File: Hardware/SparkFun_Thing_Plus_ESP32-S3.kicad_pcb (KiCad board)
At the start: 4 copper layers, 22.9 x 58.4 mm, 132 parts, among them J1 USB_C_Receptacle, J2 microSD_Friction, J3 JST_2mm_LiPo, J4 Qwiic_Vertical, SW1 4.6x2.8mm, SW2 4.6x2.8mm, U1 AP2112K-3.3, U10 ThingPlus, U2 TVS_ESD_USB, U3 ESP32-S3-MINI, U4 MAX17048, U5 MCP73831, U6 AP2112K-3.3

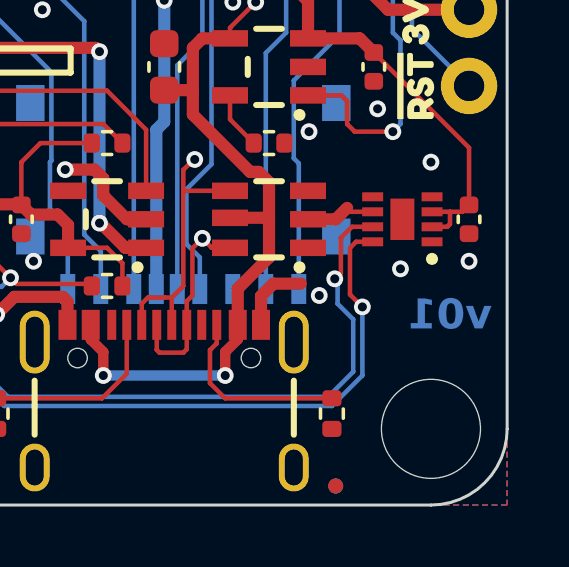
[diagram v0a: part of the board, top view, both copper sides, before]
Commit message: Remove single unit production files
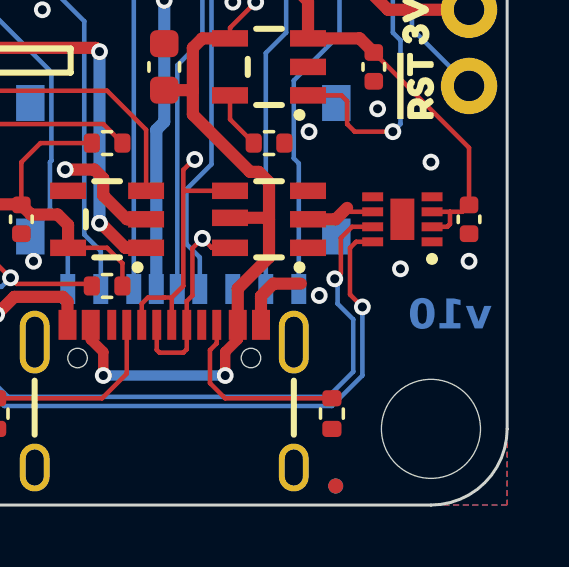
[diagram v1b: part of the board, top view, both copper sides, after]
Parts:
- removed kibuzzard-6569F804: G***, kibuzzard-6569F804
- added kibuzzard-65A403E0: G***, kibuzzard-65A403E0, B.Cu at (113.0, 98.4)
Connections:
- net +3.3V renamed 3.3V
- net +5V renamed 5V
- J3 pad NC1: (no net) -> unconnected-(J3-PadNC1)
- J3 pad NC2: (no net) -> unconnected-(J3-PadNC2)
- U4 pad 9: (no net) -> GND
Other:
- board text added: "Finish: HASL Lead-Free"
- board text added: "v10"
- board text removed: "Finish: ENIG"
- board text removed: "v01"

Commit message: Updates post review
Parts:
- removed kibuzzard-6569FC00: G***, kibuzzard-6569FC00
- removed kibuzzard-6569FC19: G***, kibuzzard-6569FC19
- removed kibuzzard-6569FC2B: G***, kibuzzard-6569FC2B
- removed kibuzzard-6569FC30: G***, kibuzzard-6569FC30
- removed kibuzzard-6569FC40: G***, kibuzzard-6569FC40
- removed kibuzzard-6569FC46: G***, kibuzzard-6569FC46
- removed kibuzzard-6569FC4B: G***, kibuzzard-6569FC4B
- removed kibuzzard-6569FC6D: G***, kibuzzard-6569FC6D
- removed kibuzzard-6569FC75: G***, kibuzzard-6569FC75
- removed kibuzzard-656A1BAC: G***, kibuzzard-656A1BAC
- removed kibuzzard-656A1BFB: G***, kibuzzard-656A1BFB
- removed kibuzzard-656A1C04: G***, kibuzzard-656A1C04
- removed kibuzzard-656A1C15: G***, kibuzzard-656A1C15
- removed kibuzzard-656A1C24: G***, kibuzzard-656A1C24
- removed kibuzzard-656A1C2E: G***, kibuzzard-656A1C2E
- removed kibuzzard-656A1C4C: G***, kibuzzard-656A1C4C
- removed kibuzzard-656A1C93: G***, kibuzzard-656A1C93
- removed kibuzzard-656A1C9C: G***, kibuzzard-656A1C9C
- removed kibuzzard-656A1CA0: G***, kibuzzard-656A1CA0
- removed kibuzzard-656A1CA7: G***, kibuzzard-656A1CA7
- removed kibuzzard-656A1CAC: G***, kibuzzard-656A1CAC
- removed kibuzzard-656A1CB7: G***, kibuzzard-656A1CB7
- removed kibuzzard-656A1CC2: G***, kibuzzard-656A1CC2
- removed kibuzzard-656A1CC7: G***, kibuzzard-656A1CC7
- removed kibuzzard-656A1CEA: G***, kibuzzard-656A1CEA
- removed kibuzzard-656A31BE: G***, kibuzzard-656A31BE
- removed kibuzzard-656A31C7: G***, kibuzzard-656A31C7
- removed kibuzzard-656A36EF: G***, kibuzzard-656A36EF
- removed kibuzzard-656A3874: G***, kibuzzard-656A3874
- removed kibuzzard-656A387C: G***, kibuzzard-656A387C
- removed kibuzzard-656A38AA: G***, kibuzzard-656A38AA
- removed kibuzzard-656A3901: G***, kibuzzard-656A3901
- added LP1: ~, SparkFun-Jumper:SMT-JUMPER_3_1-NC_TRACE_SILK, B.Cu at (116.3, 128.3)
- added Q1: DMG2305UX, SparkFun-Semiconductor-Standard:SOT23-3, F.Cu at (119.4, 129.2)
- added R17: 100k, SparkFun-Resistor:R_0402_1005Metric, F.Cu at (111.1, 139.1)
- added R18: 100k, SparkFun-Resistor:R_0402_1005Metric, F.Cu at (120.0, 131.8)
- added kibuzzard-65A9923A: G***, kibuzzard-65A9923A, B.Cu at (121.0, 100.3)
- added kibuzzard-65A99252: G***, kibuzzard-65A99252, B.Cu at (119.4, 102.9)
- added kibuzzard-65A99268: G***, kibuzzard-65A99268, B.Cu at (119.6, 105.4)
- added kibuzzard-65A9926C: G***, kibuzzard-65A9926C, B.Cu at (119.4, 108.0)
- added kibuzzard-65A9926F: G***, kibuzzard-65A9926F, B.Cu at (119.5, 110.5)
- added kibuzzard-65A99274: G***, kibuzzard-65A99274, B.Cu at (119.6, 113.0)
- added kibuzzard-65A99278: G***, kibuzzard-65A99278, B.Cu at (121.2, 115.6)
- added kibuzzard-65A9927C: G***, kibuzzard-65A9927C, B.Cu at (121.2, 118.1)
- added kibuzzard-65A9927F: G***, kibuzzard-65A9927F, B.Cu at (121.2, 120.7)
- added kibuzzard-65A99283: G***, kibuzzard-65A99283, B.Cu at (121.2, 123.2)
- added kibuzzard-65A99287: G***, kibuzzard-65A99287, B.Cu at (121.2, 125.7)
- added kibuzzard-65A9928A: G***, kibuzzard-65A9928A, B.Cu at (121.0, 128.3)
- added kibuzzard-65A9928E: G***, kibuzzard-65A9928E, B.Cu at (120.8, 130.8)
- added kibuzzard-65A99292: G***, kibuzzard-65A99292, B.Cu at (121.3, 133.3)
- added kibuzzard-65A99297: G***, kibuzzard-65A99297, B.Cu at (120.9, 135.9)
- added kibuzzard-65A992E3: G***, kibuzzard-65A992E3, B.Cu at (123.2, 141.0)
- added kibuzzard-65A99335: G***, kibuzzard-65A99335, B.Cu at (106.3, 100.3)
- added kibuzzard-65A9933C: G***, kibuzzard-65A9933C, B.Cu at (106.2, 102.9)
- added kibuzzard-65A99346: G***, kibuzzard-65A99346, B.Cu at (104.8, 108.0)
- added kibuzzard-65A9934B: G***, kibuzzard-65A9934B, B.Cu at (104.6, 105.4)
- added kibuzzard-65A99350: G***, kibuzzard-65A99350, B.Cu at (104.8, 110.5)
- added kibuzzard-65A99354: G***, kibuzzard-65A99354, B.Cu at (104.6, 113.0)
- added kibuzzard-65A99359: G***, kibuzzard-65A99359, B.Cu at (104.6, 115.6)
- added kibuzzard-65A9935C: G***, kibuzzard-65A9935C, B.Cu at (104.8, 118.1)
- added kibuzzard-65A99360: G***, kibuzzard-65A99360, B.Cu at (105.0, 120.7)
- added kibuzzard-65A99364: G***, kibuzzard-65A99364, B.Cu at (105.7, 123.2)
- added kibuzzard-65A99367: G***, kibuzzard-65A99367, B.Cu at (105.0, 125.7)
- added kibuzzard-65A9936B: G***, kibuzzard-65A9936B, B.Cu at (106.2, 128.3)
- added kibuzzard-65A9990D: G***, kibuzzard-65A9990D, F.Cu at (104.6, 123.2)
- added kibuzzard-65A99912: G***, kibuzzard-65A99912, F.Cu at (104.6, 128.3)
- added kibuzzard-65A99933: G***, kibuzzard-65A99933, B.Cu at (121.9, 96.5)
- added kibuzzard-65A99A9C: G***, kibuzzard-65A99A9C, F.Cu at (110.9, 131.2)
- added kibuzzard-65A99AA3: G***, kibuzzard-65A99AA3, F.Cu at (110.9, 136.3)
- added kibuzzard-65A99CB6: G***, kibuzzard-65A99CB6, B.Cu at (116.3, 125.3)
- added kibuzzard-65A99E72: G***, kibuzzard-65A99E72, B.Cu at (113.7, 137.4)
- C3: value 1.0uF -> 10uF; footprint SparkFun-Capacitor:C_0402_1005Metric -> SparkFun-Capacitor:C_0603_1608Metric
- U1, U6: value AP2112K-3.3 -> RT9080-3.3
- moved TP2 1.92 mm to (113.7, 130.2)
- moved R10 1.72 mm to (118.7, 147.6), turned to -90 degrees
- moved R11 1.72 mm to (107.3, 147.6), turned to 90 degrees
- turned U4 to 180 degrees
- renumbered JP1 to CHG1, JP4 to PWR1
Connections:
- net 5V renamed VIN
- C4 pad 1: 3.3V -> 3.3V_P
- C5 pad 1: 3.3V -> 3.3V_P
- C8 pad 1: 3.3V -> 3.3V_P
- D6 pad 1: 3.3V -> 3.3V_P
- J2 pad 4: 3.3V -> 3.3V_P
- R1 pad 1: 3.3V -> 3.3V_P
- R2 pad 1: 3.3V -> 3.3V_P
- R3 pad 1: 3.3V -> 3.3V_P
- R4 pad 1: 3.3V -> 3.3V_P
- R5 pad 1: 3.3V -> 3.3V_P
- R6 pad 1: 3.3V -> 3.3V_P
- U3 pad 31: unconnected-(U3-IO35-Pad31) -> ESP35/~{ALRT}
- U3 pad 37: ESP41/NC -> ESP41/LP_CTL
- U4 pad 5: unconnected-(U4-~{ALRT}-Pad5) -> ESP35/~{ALRT}
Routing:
- net 3.3V_P: track 0.00 -> 77.6 mm, vias 0 -> 9
- net ESP35/~{ALRT}: track 0.00 -> 33.5 mm, vias 0 -> 2
- net ESP41/LP_CTL: track 0.00 -> 25.1 mm, vias 0 -> 1
- net 3.3V: track 42.2 -> 21.8 mm, vias 12 -> 4
- net Net-(LP1-C): track 0.00 -> 6.60 mm, vias 0 -> 1
- net GND: track 97.6 -> 101.4 mm, vias 50 -> 54
- net ESP40/SDIO1: track 44.3 -> 47.4 mm
- net ESP39/SDIO0: track 39.9 -> 42.5 mm
- net ESP0/STAT: track 44.0 -> 46.0 mm
- net ESP~{RST}: track 54.5 -> 55.8 mm
- net Net-(CHG1-A): track 12.6 -> 11.5 mm
- net ESP47/SDIO2: track 39.2 -> 39.9 mm
- net Net-(J1-CC2): track 6.31 -> 7.06 mm
- net Net-(J1-CC1): track 6.30 -> 7.05 mm
- net Net-(D4-K): track 22.8 -> 23.3 mm
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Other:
- board text added: "Inner Copper Weight: 0.5oz"
- board text added: "Outer Copper Weight: 1oz"
- board text removed: "Copper weight: 1oz"
- board text removed: "No Clean Process"

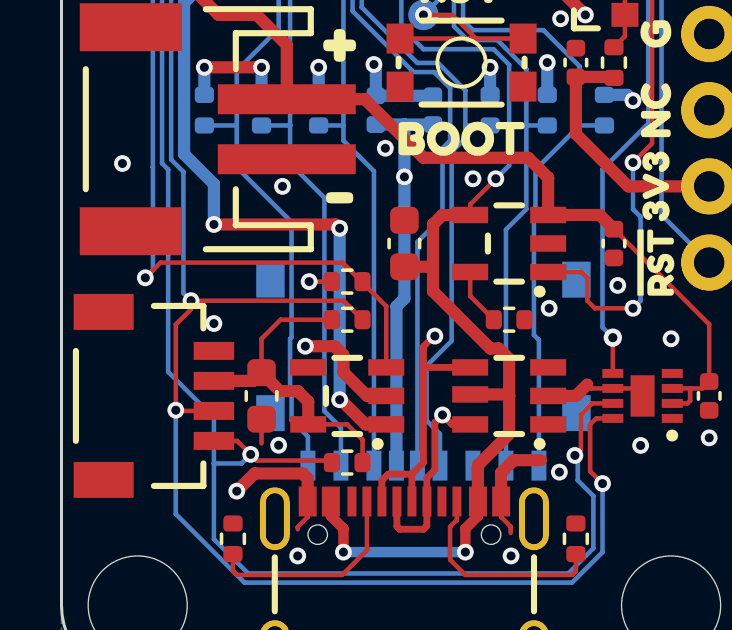
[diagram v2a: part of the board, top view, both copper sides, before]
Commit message: Add default on to Qwiic power.
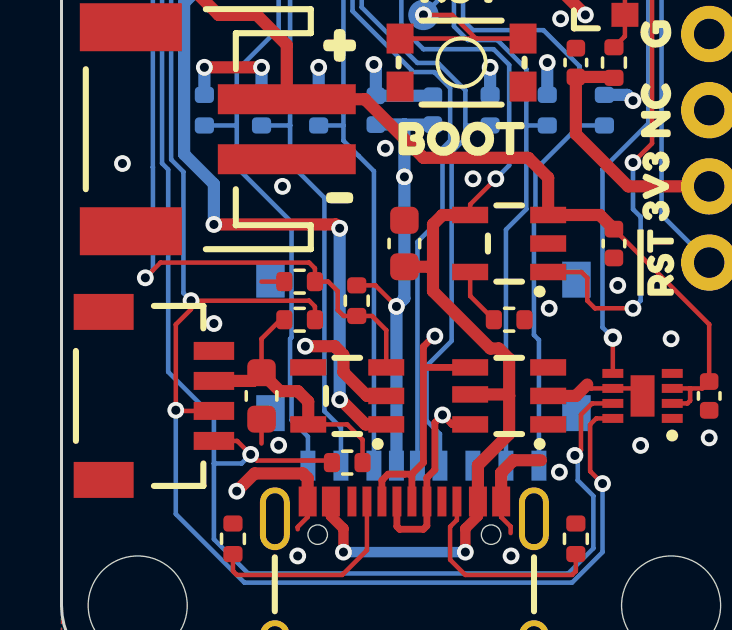
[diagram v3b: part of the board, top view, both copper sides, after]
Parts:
- removed kibuzzard-65A99CB6: G***, kibuzzard-65A99CB6
- added R19: 100k, SparkFun-Resistor:R_0402_1005Metric, F.Cu at (109.5, 139.1)
- added kibuzzard-65AA9C9F: G***, kibuzzard-65AA9C9F, B.Cu at (116.3, 123.7)
- JP1: renamed from PWR1; value ~ -> PWR
- JP2: renamed from LP1; value ~ -> LP_CTL
- R17: value 100k -> 10k
- moved R15 1.59 mm to (109.5, 140.3)
- moved R17 0.71 mm to (111.4, 139.7), turned to -90 degrees
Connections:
- R17 pad 1: GND -> 3.3V_P
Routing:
- net Q3V3: track 10.9 -> 9.23 mm
- net 3.3V_P: track 77.6 -> 79.2 mm, vias 9 -> 10
- net ESP8/SDA: track 81.4 -> 80.1 mm
- net GND: vias 54 -> 53

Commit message: Revise layout post design review
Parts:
- removed Q1: DMG2305UX, SparkFun-Semiconductor-Standard:SOT23-3
- removed R18: 100k, SparkFun-Resistor:R_0402_1005Metric
- added C14: 2.2uF, SparkFun-Capacitor:C_0402_1005Metric, F.Cu at (112.1, 144.8)
- C10: value 1.0uF -> 2.2uF
- C3: footprint SparkFun-Capacitor:C_0603_1608Metric -> SparkFun-Capacitor:C_0402_1005Metric
- JP2: footprint SparkFun-Jumper:SMT-JUMPER_3_1-NC_TRACE_SILK -> SparkFun-Jumper:SMT-JUMPER_2_NC_TRACE_SILK
- JP3: renamed from CHG1; value ~ -> CHG
- SW1, SW2: footprint SparkFun-Switch:Momentary_SMD_4.6x2.8mm -> SparkFun-Switch:Momentary_SMD_4.6x2.8mm_h2.5mm
- moved R13 5.08 mm to (107.3, 128.9), turned to 180 degrees
- moved C10 4.96 mm to (107.3, 124.5)
- moved R12 1.62 mm to (109.5, 144.8)
- moved kibuzzard-65AA9C9F 0.48 mm to (116.5, 124.1)
- moved JP2 0.19 mm to (116.5, 128.3)
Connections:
- C3 pad 1: Q3V3 -> 3.3V_P
- D6 pad 1: 3.3V_P -> Net-(D6-DOUT)
- D6 pad 2: Net-(D6-DOUT) -> GND
- D6 pad 3: GND -> ESP46/LED
- D6 pad 4: ESP46/LED -> 3.3V_P
- J4 pad 2: Q3V3 -> 3.3V_P
- JP2 pad 1: GND -> Net-(JP2-A)
- JP2 pad 2: Net-(JP2-C) -> 3.3V
- R12 pad 1: Q3V3 -> 3.3V_P
- R15 pad 1: Q3V3 -> 3.3V_P
- R17 pad 1: 3.3V_P -> Net-(JP2-A)
- U1 pad 5: Q3V3 -> 3.3V_P
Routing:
- net ESP41/LP_CTL: track 25.1 -> 0.00 mm, vias 1 -> 0
- net Net-(JP2-A): track 0.00 -> 18.4 mm, vias 0 -> 3
- net 3.3V_P: track 79.2 -> 89.3 mm
- net GND: track 101.4 -> 91.6 mm, vias 53 -> 59
- net Q3V3: track 9.23 -> 0.00 mm
- net Net-(JP2-C): track 6.60 -> 0.00 mm, vias 1 -> 0
- net VIN: track 42.8 -> 40.4 mm
- net EN: track 19.8 -> 17.5 mm, vias 3 -> 2
- net ESP9/SCL: track 77.2 -> 75.5 mm
- net ESP34/SDIO_CMD: track 37.5 -> 38.7 mm
- net ESP0/STAT: track 46.0 -> 45.0 mm
- net 3.3V: track 21.8 -> 21.4 mm, vias 4 -> 5
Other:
- board text added: "Silkscreen Color: White"

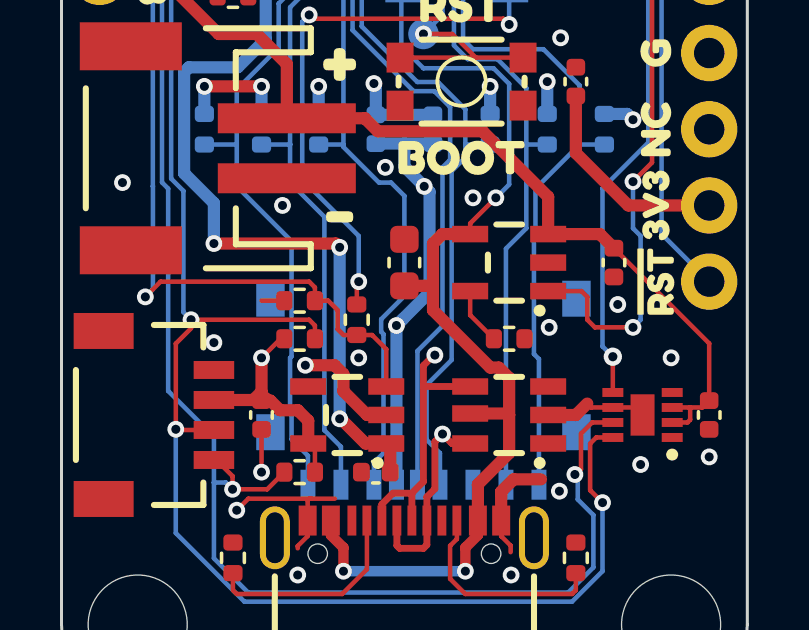
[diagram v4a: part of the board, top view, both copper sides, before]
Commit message: Fix 330 prod ID. Update parts to new naming conventions
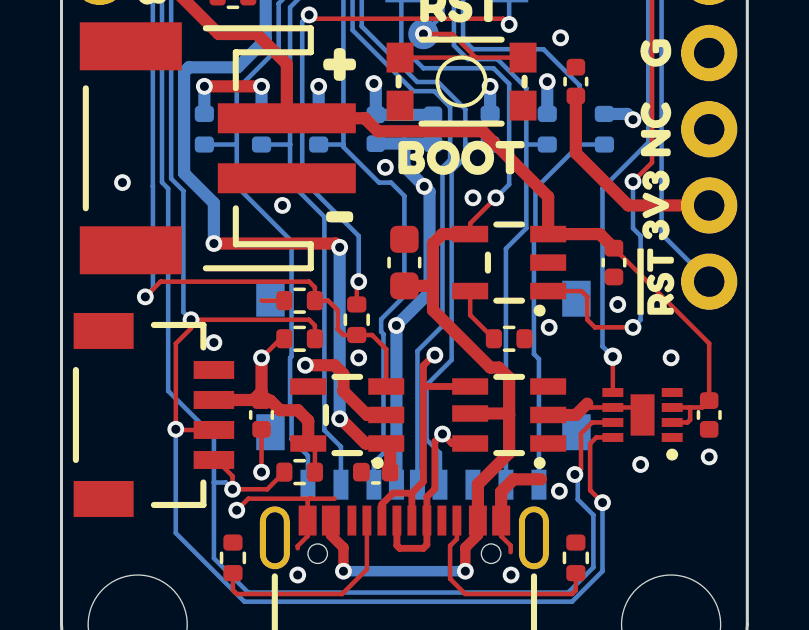
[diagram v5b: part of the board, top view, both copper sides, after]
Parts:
- D2, D3: value 3A -> BAT60A
- FID1, FID2, FID3, FID4: value Fiducial_0.5 -> Fiducial_0.5mm
- J1: footprint SparkFun-Connector:USB-C-16P -> SparkFun-Connector:USB-C_16
- J3: footprint SparkFun-Connector:JST-2-SMD -> SparkFun-Connector:JST_SMD_2.0mm-2
- J4: value Qwiic_Vertical -> Qwiic_RA; footprint SparkFun-Connector:JST04_1MM_RA -> SparkFun-Connector:JST_SMD_1.0mm-4_RA
- JP1: value PWR -> ~; footprint SparkFun-Jumper:SMT-JUMPER_2_NC_TRACE_SILK -> SparkFun-Jumper:Jumper_2_NC_Trace
- JP2: value LP_CTL -> ~; footprint SparkFun-Jumper:SMT-JUMPER_2_NC_TRACE_SILK -> SparkFun-Jumper:Jumper_2_NC_Trace
- JP3: value CHG -> ~; footprint SparkFun-Jumper:SMT-JUMPER_2_NC_TRACE_SILK -> SparkFun-Jumper:Jumper_2_NC_Trace
- ST1, ST3: value Stand_off -> Standoff; footprint SparkFun-Hardware:STAND-OFF -> SparkFun-Hardware:Standoff
- SW1, SW2: value 4.6x2.8mm -> SMD_4.6x2.8mm_h2.5mm
- U2: value TVS_ESD_USB -> DT1042-04SO
- U9: footprint SparkFun-Aesthetic:ORDERING_INSTRUCTIONS -> SparkFun-Aesthetic:Ordering_Instructions

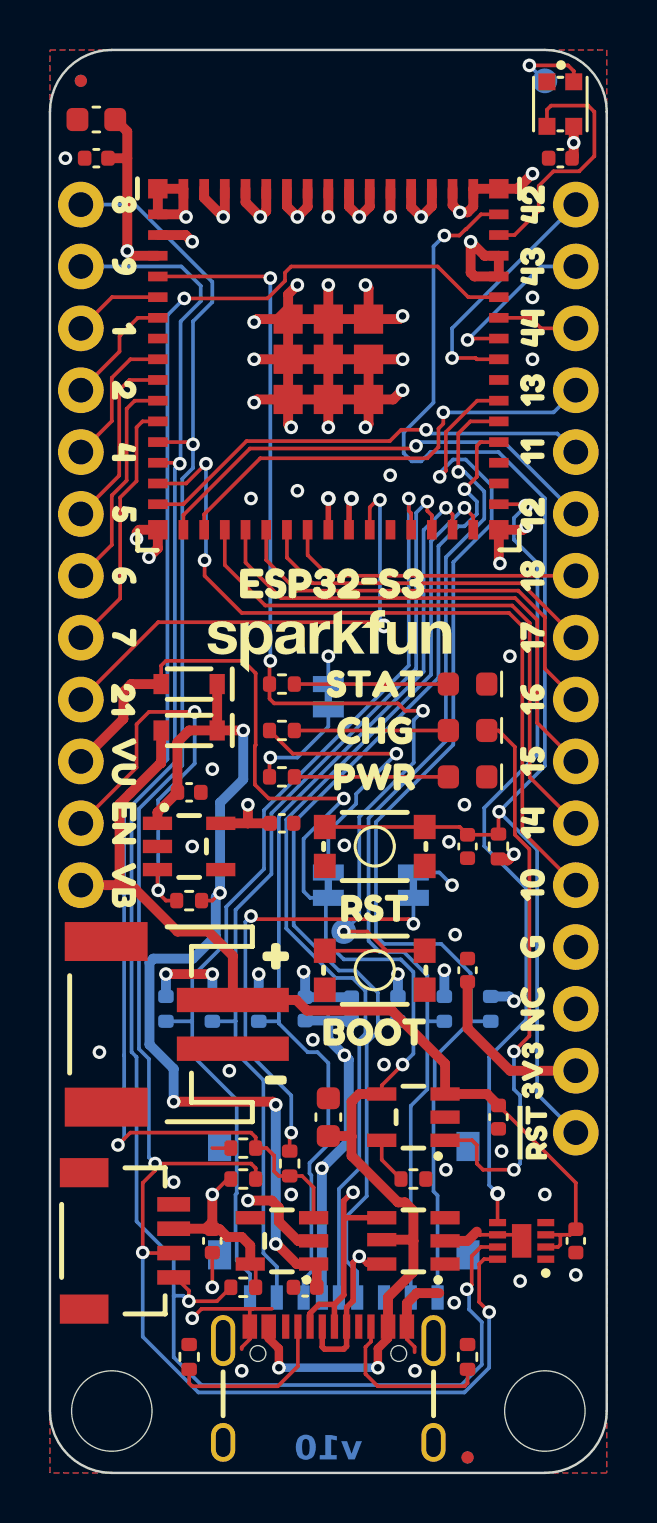
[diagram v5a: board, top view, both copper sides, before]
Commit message: Update with current models and symbols
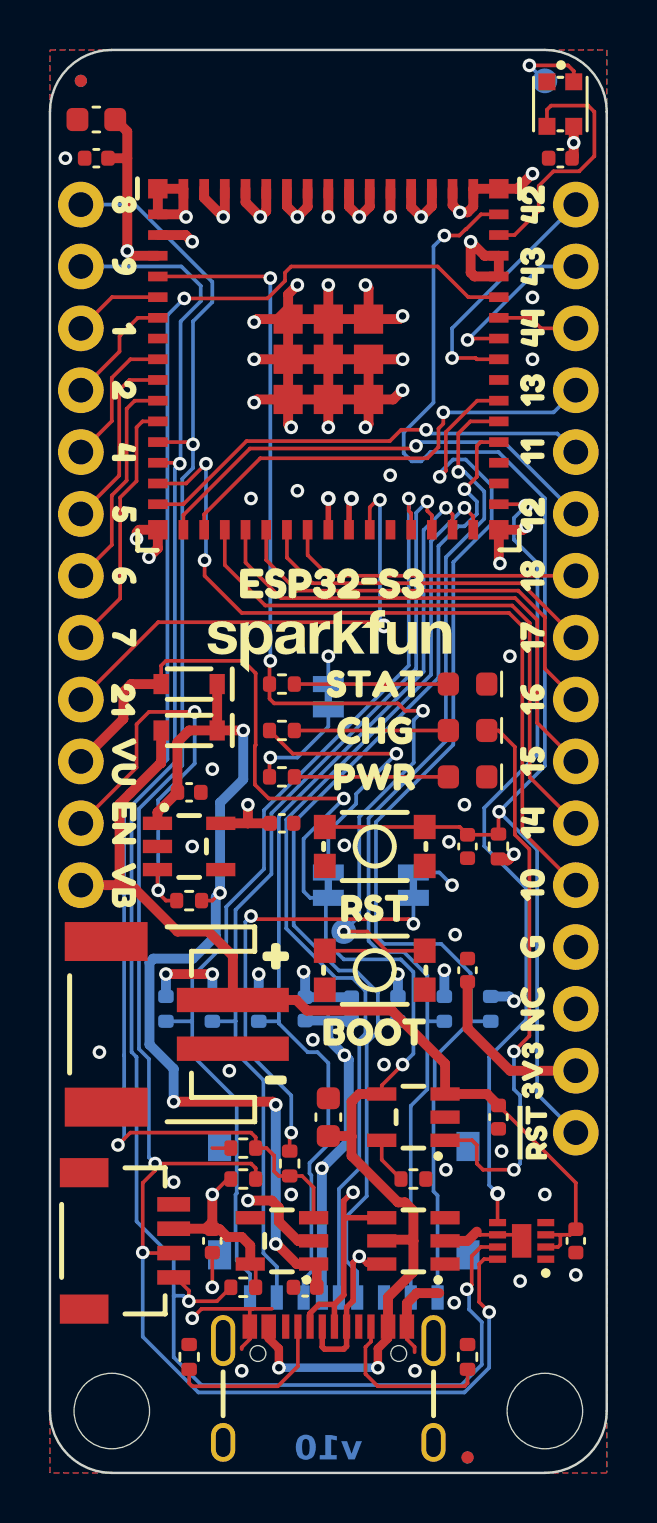
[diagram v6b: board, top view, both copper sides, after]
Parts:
- D1: footprint SparkFun-LED:LED_0603_1608Metric -> SparkFun-LED:LED_0603_1608Metric_Green
- D4: footprint SparkFun-LED:LED_0603_1608Metric -> SparkFun-LED:LED_0603_1608Metric_Yellow
- D5: footprint SparkFun-LED:LED_0603_1608Metric -> SparkFun-LED:LED_0603_1608Metric_Red
- D6: footprint SparkFun-LED:WS2812-2020 -> SparkFun-LED:WS2812_2020
- J2: footprint SparkFun-Connector:microSD_Friction_Fit_Atom -> SparkFun-Connector:microSD_Friction_Fit_Common
- SW1, SW2: footprint SparkFun-Switch:Momentary_SMD_4.6x2.8mm_h2.5mm -> SparkFun-Switch:Push_SMD_4.6x2.8mm_h2.5mm
